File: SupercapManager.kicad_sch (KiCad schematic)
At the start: 5 parts, among them J1 JST4_M, J2 XT30_M, J3 XT30_M, J4 XT30_M, J5 XT30_M

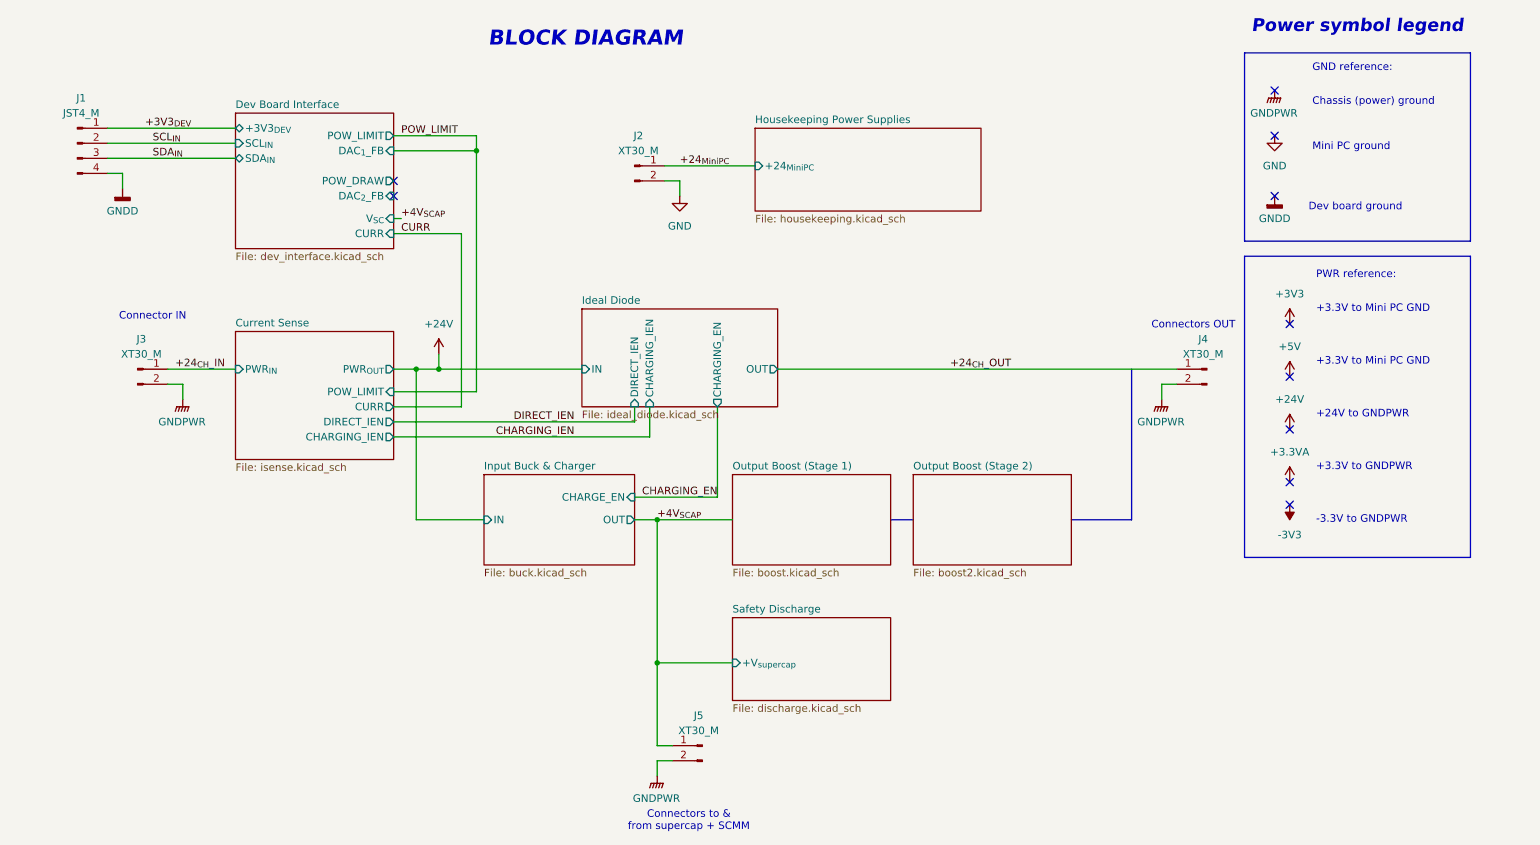
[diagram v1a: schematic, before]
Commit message: Completed stage 2 schematic
+ added SPICE models for all the custom components
+ renumbered components
+ updated library with stage 2 symbols
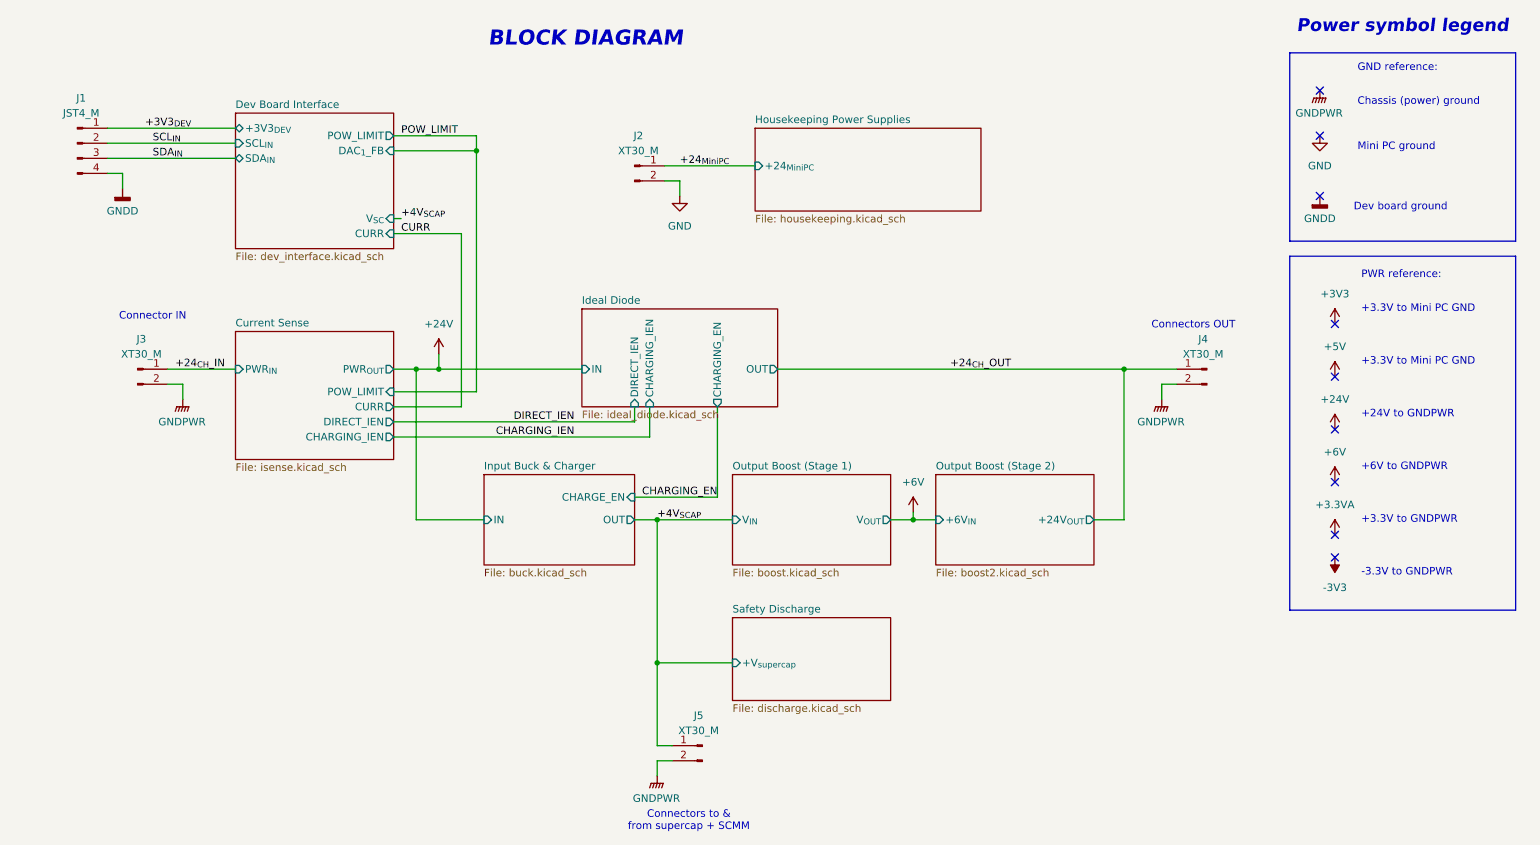
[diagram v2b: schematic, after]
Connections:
- no-connect marks 10 -> 9
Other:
- sheet Dev Board Interface ports: added none; removed DAC_{2}_FB, POW_DRAW
- sheet Output Boost (Stage 1) ports: added V_{IN}, V_{OUT}; removed none
- sheet Output Boost (Stage 2) ports: added +24V_{OUT}, +6V_{IN}; removed none
- note added: "+6V to GNDPWR"

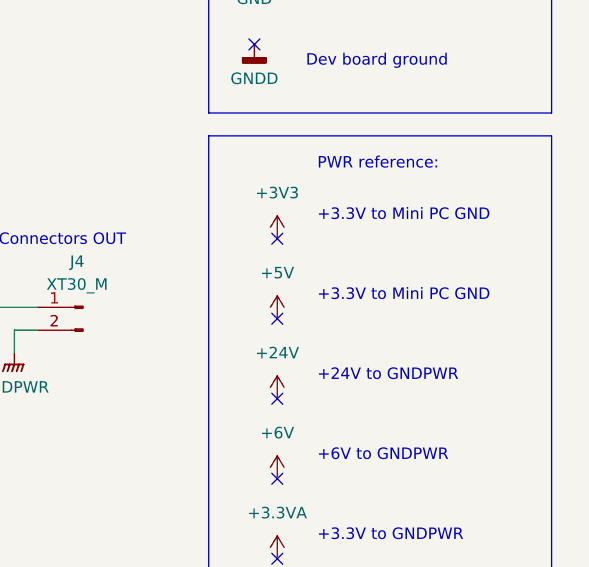
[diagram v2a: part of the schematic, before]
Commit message: Implement SPICE'd circuits in KiCAD
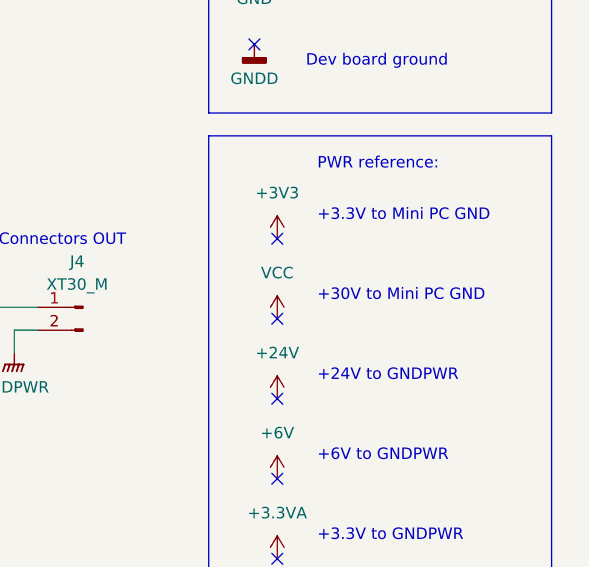
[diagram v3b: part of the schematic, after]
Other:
- note added: "+30V to Mini PC GND"
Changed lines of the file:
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@@
 		)
 	)
-	(text "+3.3V to Mini PC GND"
+	(text "+30V to Mini PC GND"
 		(exclude_from_sim no)
 		(at 245.745 92.71 0)
@@
 	)
 	(symbol
-		(lib_id "power:+5V")
+		(lib_id "power:+6V")
+		(at 241.3 113.03 0)
+		(unit 1)
+		(exclude_from_sim no)
+		(in_bom yes)
+		(on_board yes)
+		(dnp no)
+		(fields_autoplaced yes)
+		(property "Reference" "#PWR021"
+			(at 241.3 116.84 0)
+			(effects
+				(font
+					(size 1.27 1.27)
+				)
+				(hide yes)
+			)
+		)
+		(property "Value" "+6V"
+			(at 241.3 107.95 0)
+			(effects
+				(font
+					(size 1.27 1.27)
+				)
+			)
+		)
+		(property "Footprint" ""
+			(at 241.3 113.03 0)
+			(effects
+				(font
+					(size 1.27 1.27)
+				)
+				(hide yes)
+			)
+		)
+		(property "Datasheet" ""
+			(at 241.3 113.03 0)
+			(effects
+				(font
+					(size 1.27 1.27)
+				)
+				(hide yes)
+			)
+		)
+		(property "Description" "Power symbol creates a global label with name \"+6V\""
+			(at 241.3 113.03 0)
+			(effects
+				(font
+					(size 1.27 1.27)
+				)
+				(hide yes)
+			)
+		)
+		(pin "1"
+		)
+		(instances
+			(project "SupercapManager"
+				(path "/6197145b-e7d4-44cc-9d90-537b6501bf60"
+					(reference "#PWR021")
+					(unit 1)
+				)
+			)
+		)
+	)
+	(symbol
+		(lib_id "power:+3V3")
+		(at 241.3 86.36 0)
+		(unit 1)
+		(exclude_from_sim no)
+		(in_bom yes)
+		(on_board yes)
+		(dnp no)
+		(fields_autoplaced yes)
+		(property "Reference" "#PWR06"
+			(at 241.3 90.17 0)
+			(effects
+				(font
+					(size 1.27 1.27)
+				)
+				(hide yes)
+			)
+		)
+		(property "Value" "+3V3"
+			(at 241.3 81.28 0)
+			(effects
+				(font
+					(size 1.27 1.27)
+				)
+			)
+		)
+		(property "Footprint" ""
+			(at 241.3 86.36 0)
+			(effects
+				(font
+					(size 1.27 1.27)
+				)
+				(hide yes)
+			)
+		)
+		(property "Datasheet" ""
+			(at 241.3 86.36 0)
+			(effects
+				(font
+					(size 1.27 1.27)
+				)
+				(hide yes)
+			)
+		)
+		(property "Description" "Power symbol creates a global label with name \"+3V3\""
+			(at 241.3 86.36 0)
+			(effects
+				(font
+					(size 1.27 1.27)
+				)
+				(hide yes)
+			)
+		)
+		(pin "1"
+		)
+		(instances
+			(project ""
+				(path "/6197145b-e7d4-44cc-9d90-537b6501bf60"
+					(reference "#PWR06")
+					(unit 1)
+				)
+			)
+		)
+	)
+	(symbol
+		(lib_id "power:VCC")
 		(at 241.3 95.25 0)
 		(unit 1)
@@
 			)
 		)
-		(property "Value" "+5V"
+		(property "Value" "VCC"
 			(at 241.3 90.17 0)
 			(effects
@@
 			)
 		)
-		(property "Description" "Power symbol creates a global label with name \"+5V\""
+		(property "Description" "Power symbol creates a global label with name \"VCC\""
 			(at 241.3 95.25 0)
 			(effects
@@
 					(unit 1)
 				)
-			)
-		)
-	)
-	(symbol
-		(lib_id "power:+6V")
-		(at 241.3 113.03 0)
-		(unit 1)
-		(exclude_from_sim no)
-		(in_bom yes)
-		(on_board yes)
-		(dnp no)
-		(fields_autoplaced yes)
-		(property "Reference" "#PWR021"
-			(at 241.3 116.84 0)
-			(effects
-				(font
-					(size 1.27 1.27)
-				)
-				(hide yes)
-			)
-		)
-		(property "Value" "+6V"
-			(at 241.3 107.95 0)
-			(effects
-				(font
-					(size 1.27 1.27)
-				)
-			)
-		)
-		(property "Footprint" ""
-			(at 241.3 113.03 0)
-			(effects
-				(font
-					(size 1.27 1.27)
-				)
-				(hide yes)
-			)
-		)
-		(property "Datasheet" ""
-			(at 241.3 113.03 0)
-			(effects
-				(font
-					(size 1.27 1.27)
-				)
-				(hide yes)
-			)
-		)
-		(property "Description" "Power symbol creates a global label with name \"+6V\""
-			(at 241.3 113.03 0)
-			(effects
-				(font
-					(size 1.27 1.27)
-				)
-				(hide yes)
-			)
-		)
-		(pin "1"
-		)
-		(instances
-			(project "SupercapManager"
-				(path "/6197145b-e7d4-44cc-9d90-537b6501bf60"
-					(reference "#PWR021")
-					(unit 1)
-				)
-			)
-		)
-	)
-	(symbol
-		(lib_id "power:+3V3")
-		(at 241.3 86.36 0)
-		(unit 1)
-		(exclude_from_sim no)
-		(in_bom yes)
-		(on_board yes)
-		(dnp no)
-		(fields_autoplaced yes)
-		(property "Reference" "#PWR06"
-			(at 241.3 90.17 0)
-			(effects
-				(font
-					(size 1.27 1.27)
-				)
-				(hide yes)
-			)
-		)
-		(property "Value" "+3V3"
-			(at 241.3 81.28 0)
-			(effects
-				(font
-					(size 1.27 1.27)
-				)
-			)
-		)
-		(property "Footprint" ""
-			(at 241.3 86.36 0)
-			(effects
-				(font
-					(size 1.27 1.27)
-				)
-				(hide yes)
-			)
-		)
-		(property "Datasheet" ""
-			(at 241.3 86.36 0)
-			(effects
-				(font
-					(size 1.27 1.27)
-				)
-				(hide yes)
-			)
-		)
-		(property "Description" "Power symbol creates a global label with name \"+3V3\""
-			(at 241.3 86.36 0)
-			(effects
-				(font
-					(size 1.27 1.27)
-				)
-				(hide yes)
-			)
-		)
-		(pin "1"
-		)
-		(instances
-			(project ""
-				(path "/6197145b-e7d4-44cc-9d90-537b6501bf60"
-					(reference "#PWR06")
-					(unit 1)
-				)

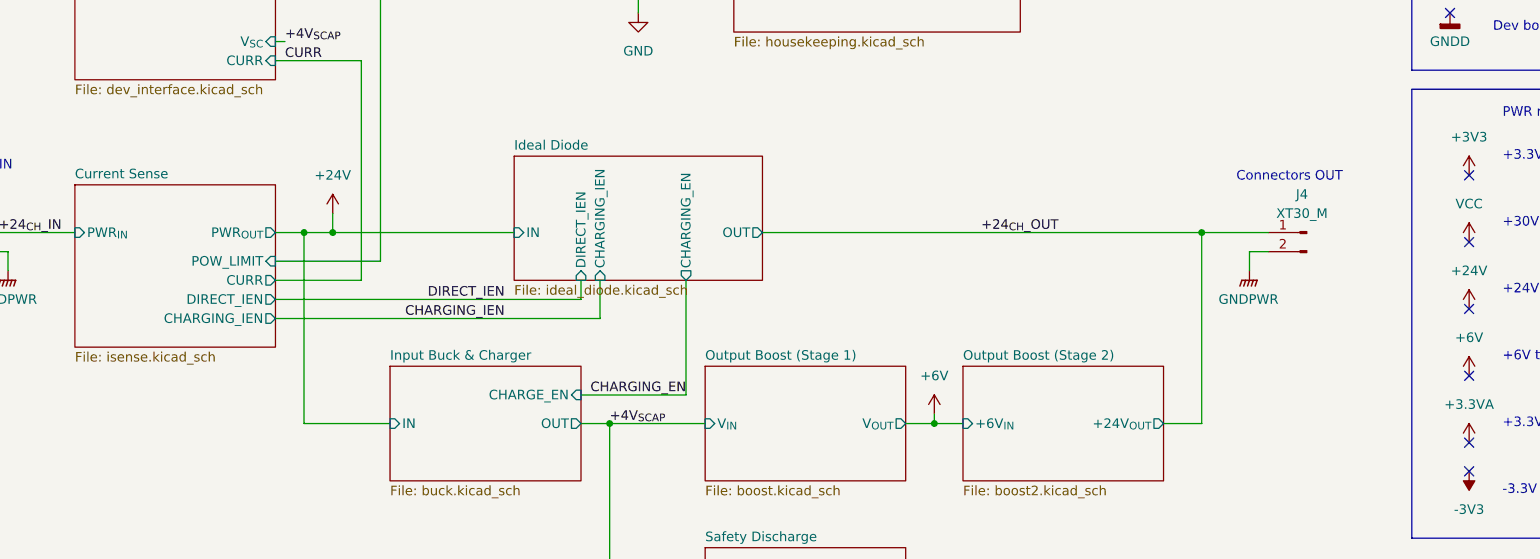
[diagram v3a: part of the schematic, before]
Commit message: Completed block diagram
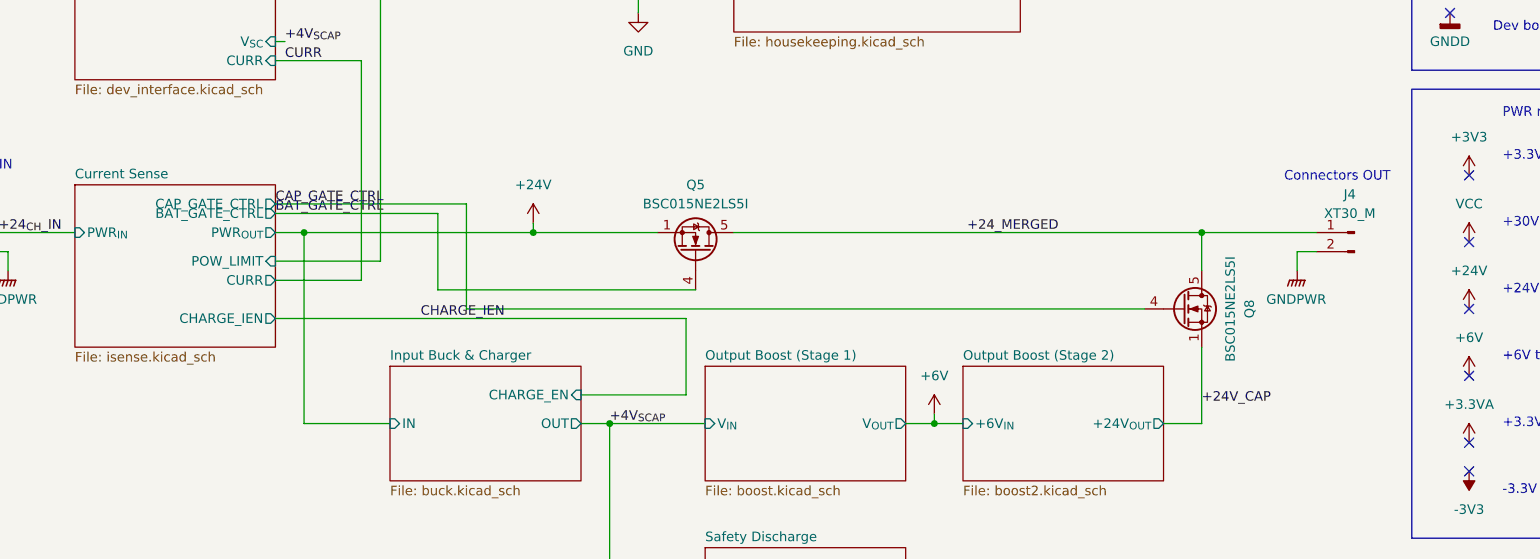
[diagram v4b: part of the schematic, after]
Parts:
- added Q5, Q8: BSC015NE2LS5I, Package_TO_SOT_SMD:TDSON-8-1, symbol Transistor_FET:BSC026N08NS5
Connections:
- net +24V: now also Q5.1 (S), Q5.2 (S), Q5.3 (S)
- net +24_{CH}_OUT renamed +24_MERGED
- net +24_MERGED: now also Q5.5 (D), Q8.5 (D)
- new net +24V_CAP: Q8.1 (S), Q8.2 (S), Q8.3 (S)
- new net BAT_GATE_CTRL: Q5.4 (G)
- new net CAP_GATE_CTRL: Q8.4 (G)
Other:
- removed sheet Ideal Diode
- sheet Current Sense ports: added BAT_GATE_CTRL, CAP_GATE_CTRL, CHARGE_IEN; removed CHARGING_IEN, DIRECT_IEN
- moved on the sheet: J4

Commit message: Add note for self
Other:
- note added: "TODO: Make this prettier lol"
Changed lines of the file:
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@@
+		)
+	)
+	(text "TODO: Make this prettier lol"
+		(exclude_from_sim no)
+		(at 164.846 89.154 0)
+		(effects
+			(font
+				(size 1.27 1.27)
+			)
+			(justify bottom)
 		)
 	)

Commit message: Redesign housekeeping supplies
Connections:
- net +24_{CH}_IN renamed +24_IN
- no-connect marks 9 -> 7
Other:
- note removed: "+3.3V to GNDPWR"
- note removed: "-3.3V to GNDPWR"
- moved on the sheet: J5

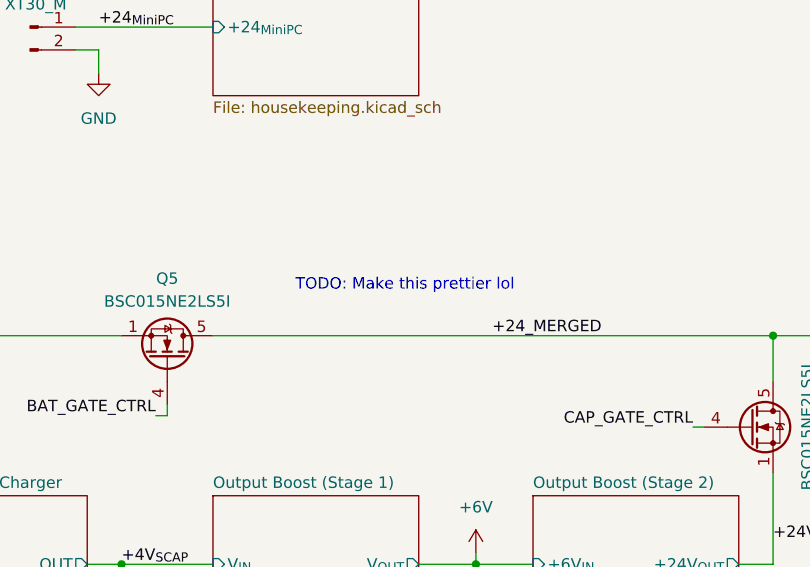
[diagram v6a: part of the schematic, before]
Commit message: Properly spec 30V output
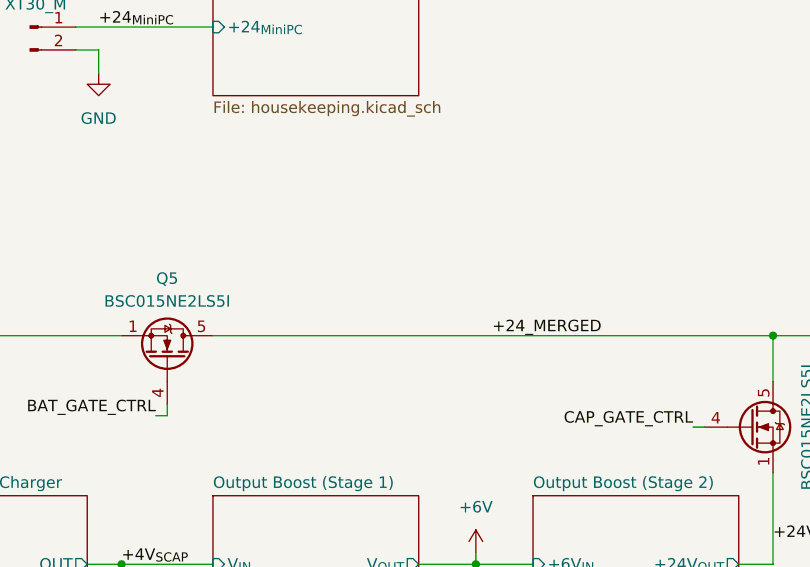
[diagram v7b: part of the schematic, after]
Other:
- note removed: "TODO: Make this prettier lol"
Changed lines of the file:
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@@
-		)
-	)
-	(text "TODO: Make this prettier lol"
-		(exclude_from_sim no)
-		(at 164.846 89.154 0)
-		(effects
-			(font
-				(size 1.27 1.27)
-			)
-			(justify bottom)
 		)
 	)
@@
 			(project "SupercapManager"
 				(path "/6197145b-e7d4-44cc-9d90-537b6501bf60"
-					(page "8")
+					(page "7")
 				)
 			)
@@
 			(project "SupercapManager"
 				(path "/6197145b-e7d4-44cc-9d90-537b6501bf60"
-					(page "9")
-				)
-			)
+					(page "8")
+				)
+			)
